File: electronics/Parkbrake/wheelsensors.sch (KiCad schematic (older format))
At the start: 52 parts, among them Q33 NX3008CBKS, U31 MAX232, U32 MAX232, U33 NCV1124, U34 NCV1124, U35 74LVC08

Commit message: some more work on parkbrake pcb
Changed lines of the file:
@@
 $EndComp
 $Comp
-L GND #PWR105
+L GND #PWR0103
 U 1 1 579010CB
 P 6975 3825
-F 0 "#PWR105" H 6975 3575 50  0001 C CNN
+F 0 "#PWR0103" H 6975 3575 50  0001 C CNN
 F 1 "GND" H 6975 3675 50  0001 C CNN
 F 2 "" H 6975 3825 50  0000 C CNN
@@
 $EndComp
 $Comp
-L GND #PWR103
+L GND #PWR0104
 U 1 1 57901107
 P 6225 3300
-F 0 "#PWR103" H 6225 3050 50  0001 C CNN
+F 0 "#PWR0104" H 6225 3050 50  0001 C CNN
 F 1 "GND" H 6225 3150 50  0000 C CNN
 F 2 "" H 6225 3300 50  0000 C CNN
@@
 $EndComp
 $Comp
-L GND #PWR98
+L GND #PWR0105
 U 1 1 579017A6
 P 5925 2700
-F 0 "#PWR98" H 5925 2450 50  0001 C CNN
+F 0 "#PWR0105" H 5925 2450 50  0001 C CNN
 F 1 "GND" H 5925 2550 50  0001 C CNN
 F 2 "" H 5925 2700 50  0000 C CNN
@@
 $EndComp
 $Comp
-L GND #PWR96
+L GND #PWR0106
 U 1 1 57901C47
 P 5875 3500
-F 0 "#PWR96" H 5875 3250 50  0001 C CNN
+F 0 "#PWR0106" H 5875 3250 50  0001 C CNN
 F 1 "GND" H 5875 3350 50  0000 C CNN
 F 2 "" H 5875 3500 50  0000 C CNN
@@
 $EndComp
 $Comp
-L GND #PWR106
+L GND #PWR0107
 U 1 1 57902641
 P 10075 5525
-F 0 "#PWR106" H 10075 5275 50  0001 C CNN
+F 0 "#PWR0107" H 10075 5275 50  0001 C CNN
 F 1 "GND" H 10075 5375 50  0000 C CNN
 F 2 "" H 10075 5525 50  0000 C CNN
@@
 $EndComp
 $Comp
-L GND #PWR104
+L GND #PWR0108
 U 1 1 579039CC
 P 6925 2175
-F 0 "#PWR104" H 6925 1925 50  0001 C CNN
+F 0 "#PWR0108" H 6925 1925 50  0001 C CNN
 F 1 "GND" H 6925 2025 50  0001 C CNN
 F 2 "" H 6925 2175 50  0000 C CNN
@@
 $EndComp
 $Comp
-L GND #PWR102
+L GND #PWR0109
 U 1 1 579039D2
 P 6225 1675
-F 0 "#PWR102" H 6225 1425 50  0001 C CNN
+F 0 "#PWR0109" H 6225 1425 50  0001 C CNN
 F 1 "GND" H 6225 1525 50  0000 C CNN
 F 2 "" H 6225 1675 50  0000 C CNN
@@
 $EndComp
 $Comp
-L GND #PWR97
+L GND #PWR0110
 U 1 1 57903A09
 P 5925 1075
-F 0 "#PWR97" H 5925 825 50  0001 C CNN
+F 0 "#PWR0110" H 5925 825 50  0001 C CNN
 F 1 "GND" H 5925 925 50  0001 C CNN
 F 2 "" H 5925 1075 50  0000 C CNN
@@
 $EndComp
 $Comp
-L GND #PWR95
+L GND #PWR0111
 U 1 1 57903A27
 P 5875 1875
-F 0 "#PWR95" H 5875 1625 50  0001 C CNN
+F 0 "#PWR0111" H 5875 1625 50  0001 C CNN
 F 1 "GND" H 5875 1725 50  0000 C CNN
 F 2 "" H 5875 1875 50  0000 C CNN
@@
 $EndComp
 $Comp
-L GND #PWR93
+L GND #PWR0112
 U 1 1 57907ABF
 P 3075 5550
-F 0 "#PWR93" H 3075 5300 50  0001 C CNN
+F 0 "#PWR0112" H 3075 5300 50  0001 C CNN
 F 1 "GND" H 3075 5400 50  0001 C CNN
 F 2 "" H 3075 5550 50  0000 C CNN
@@
 $EndComp
 $Comp
-L GND #PWR94
+L GND #PWR0113
 U 1 1 5790981F
 P 3125 7025
-F 0 "#PWR94" H 3125 6775 50  0001 C CNN
+F 0 "#PWR0113" H 3125 6775 50  0001 C CNN
 F 1 "GND" H 3125 6875 50  0000 C CNN
 F 2 "" H 3125 7025 50  0000 C CNN
@@
 $EndComp
 $Comp
-L GND #PWR92
+L GND #PWR0114
 U 1 1 5790996D
 P 2925 6350
-F 0 "#PWR92" H 2925 6100 50  0001 C CNN
+F 0 "#PWR0114" H 2925 6100 50  0001 C CNN
 F 1 "GND" H 2925 6200 50  0001 C CNN
 F 2 "" H 2925 6350 50  0000 C CNN
@@
 $EndComp
 $Comp
-L GND #PWR100
+L GND #PWR0115
 U 1 1 5790C737
 P 6125 5550
-F 0 "#PWR100" H 6125 5300 50  0001 C CNN
+F 0 "#PWR0115" H 6125 5300 50  0001 C CNN
 F 1 "GND" H 6125 5400 50  0001 C CNN
 F 2 "" H 6125 5550 50  0000 C CNN
@@
 $EndComp
 $Comp
-L GND #PWR101
+L GND #PWR0116
 U 1 1 5790C770
 P 6175 7025
-F 0 "#PWR101" H 6175 6775 50  0001 C CNN
+F 0 "#PWR0116" H 6175 6775 50  0001 C CNN
 F 1 "GND" H 6175 6875 50  0000 C CNN
 F 2 "" H 6175 7025 50  0000 C CNN
@@
 $EndComp
 $Comp
-L GND #PWR99
+L GND #PWR0117
 U 1 1 5790C776
 P 5975 6350
-F 0 "#PWR99" H 5975 6100 50  0001 C CNN
+F 0 "#PWR0117" H 5975 6100 50  0001 C CNN
 F 1 "GND" H 5975 6200 50  0001 C CNN
 F 2 "" H 5975 6350 50  0000 C CNN
@@
 +3.3V
 $Comp
-L GND #PWR107
+L GND #PWR0118
 U 1 1 5795B22F
 P 10100 1450
-F 0 "#PWR107" H 10100 1200 50  0001 C CNN
+F 0 "#PWR0118" H 10100 1200 50  0001 C CNN
 F 1 "GND" H 10100 1300 50  0001 C CNN
 F 2 "" H 10100 1450 50  0000 C CNN
@@
 Wire Notes Line
 	5500 2800 5225 2800
+Text GLabel 5175 3725 2    60   Input ~ 0
+SensorGND
 $EndSCHEMATC

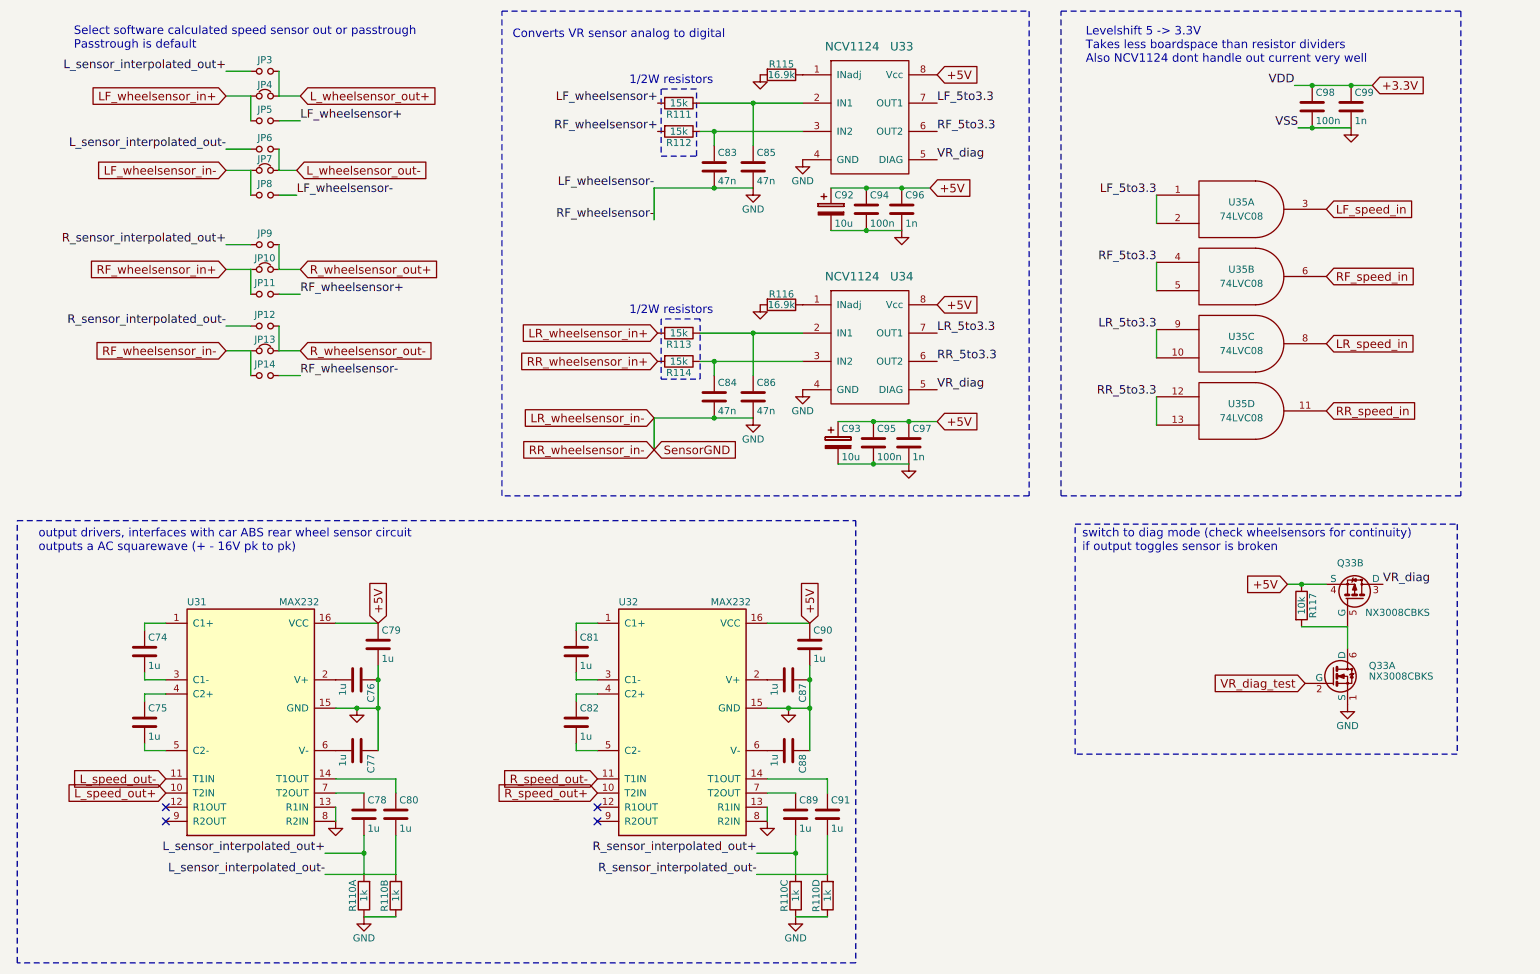
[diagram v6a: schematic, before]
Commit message: More work on inputs and 5 volt
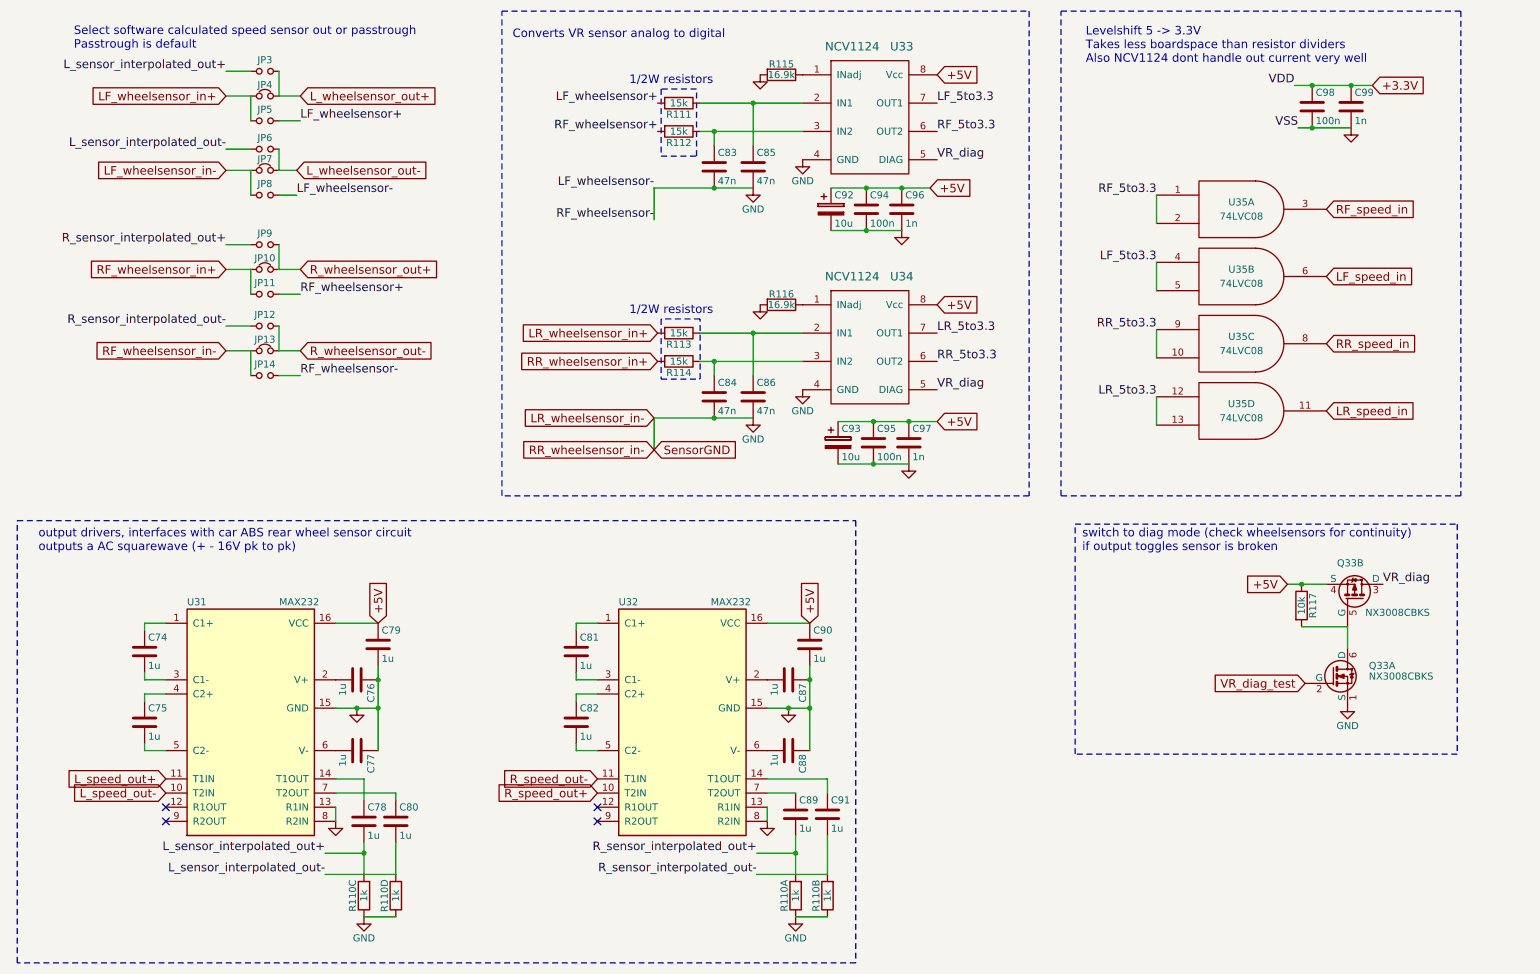
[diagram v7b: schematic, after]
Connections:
- net GND: now also R110.1, R110.2, R110.3, R110.4; no longer R110.1, R110.2, R110.3, R110.4
- net LF_5to3.3: now also U35.4, U35.5; no longer U35.1, U35.2
- net LF_speed_in: now also U35.6; no longer U35.3
- net LR_5to3.3: now also U35.12, U35.13; no longer U35.10, U35.9
- net LR_speed_in: now also U35.11; no longer U35.8
- net L_sensor_interpolated_out+: now also R110.6; no longer R110.8
- net L_sensor_interpolated_out-: now also R110.5; no longer R110.7
- net L_speed_out+: now also U31.11 (T1IN); no longer U31.10 (T2IN)
- net L_speed_out-: now also U31.10 (T2IN); no longer U31.11 (T1IN)
- net RF_5to3.3: now also U35.1, U35.2; no longer U35.4, U35.5
- net RF_speed_in: now also U35.3; no longer U35.6
- net RR_5to3.3: now also U35.10, U35.9; no longer U35.12, U35.13
- net RR_speed_in: now also U35.8; no longer U35.11
- net R_sensor_interpolated_out+: now also R110.8; no longer R110.6
- net R_sensor_interpolated_out-: now also R110.7; no longer R110.5
- net at U31.14 (T1OUT): now also C78.1; no longer C80.1
- net at U31.7 (T2OUT): now also C80.1; no longer C78.1
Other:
- moved on the sheet: C78, C80
